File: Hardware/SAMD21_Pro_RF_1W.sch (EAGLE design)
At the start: 77 parts, among them J10 AVR_SPI_PROG_3X2TESTPOINTS, J12 JST, J13 U.FL, J14 RFM_DIO, J7 PTH, J9 External On/Off, U1 MCP73831, U2 ADJ3.3, U4 ATSAMD21G, U5 4MB Flash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

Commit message: Updates from board review
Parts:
- removed F2: 6V/0.75A, SparkFun-Fuses:PPTC_THREE-QUARTER-AMP
- removed J14: RFM_DIO, SparkFun-Connectors:CONN_06X2NO_SILK
- removed JP1, JP2: JUMPER-SMT_2_NO_SILK, SparkFun-Jumpers:JUMPER-SMT_2_NO_SILK
- removed JP3: JUMPER-SMT_3_1-NC_PASTE_SILK, SparkFun-Jumpers:JUMPER-SMT_3_1-NC_PASTE_SILK
- removed JP6: JUMPER-SMT_2_NC_PASTE_SILK, SparkFun-Jumpers:JUMPER-SMT_2_NC_PASTE_SILK
- removed LED2: RED, SparkFun-LED:LED-RED0603
- removed R12: 1k, SparkFun-Resistors:1KOHM-0603-1/10W-1%
- D4: value Yellow -> BLUE; device SparkFun-LED:LED-YELLOW0603 -> SparkFun-LED:LED-BLUE0603
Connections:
- removed net ANT_HEADER: J4.1, JP3.1
- removed net DIO0: J14.11, JP6.1, U8.A7
- removed net DIO1: J14.9, JP1.1, U8.A8
- removed net DIO2: J14.7, JP2.1, U9.A4
- removed net DIO3: J14.5, U9.A3
- removed net DIO35V: U6.DIO3, U9.B3
- removed net DIO4: J14.3, U9.A2
- removed net DIO45V: U6.DIO4, U9.B2
- removed net DIO5: J14.1, U9.A1
- removed net DIO55V: U6.DIO5, U9.B1
- removed net N$10: LED2.A, R12.1
- removed net N$3: J13.SIGNAL, JP3.3
- removed net N$4: F2.2, U2.IN
- net 5V: no longer R12.2
- net ANT: now also J13.SIGNAL, J4.1; no longer JP3.2
- net D10: now also U8.A8; no longer JP1.2
- net D11: now also U9.A4; no longer JP2.2
- net GND: no longer J14.10, J14.12, J14.2, J14.4, J14.6, J14.8, LED2.C
- net N$12: now also F1.1, SJ2.2; no longer F1.2, U7.IN
- net RAW: now also U2.IN, U7.IN; no longer F1.1, F2.1
- net RFM_INT: now also U8.A7; no longer JP6.2
- net USB_VCC: now also F1.2; no longer SJ2.2
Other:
- note added: "Elias Santistevan, Owen Lyke"
- note removed: "Close jumpers for LoRa WAN compatibility"
- note removed: "Elias Santistevan"
- note removed: "Pretty confident the E19 module uses the same base chip as the RFM (hope RF version) meaning that the DIO functions are the same"
- note removed: "Why were PB22 and PB23 left unconnected in other versions?"
- moved on the sheet: F1

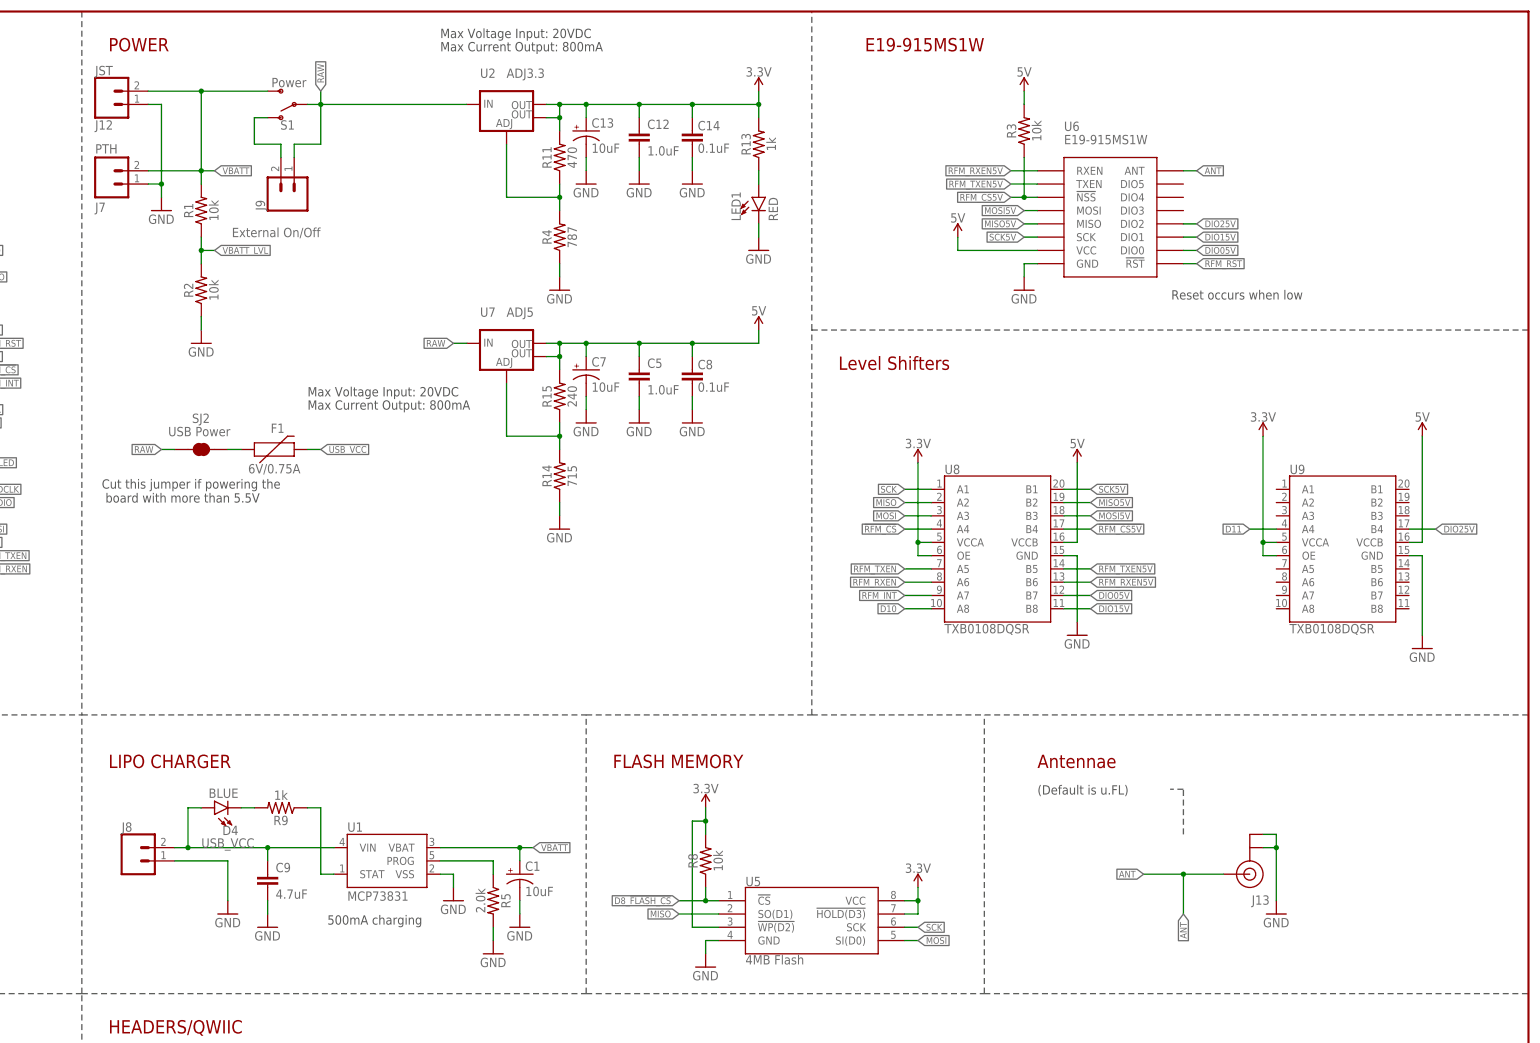
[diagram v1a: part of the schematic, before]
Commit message: Updated power supply in schematic
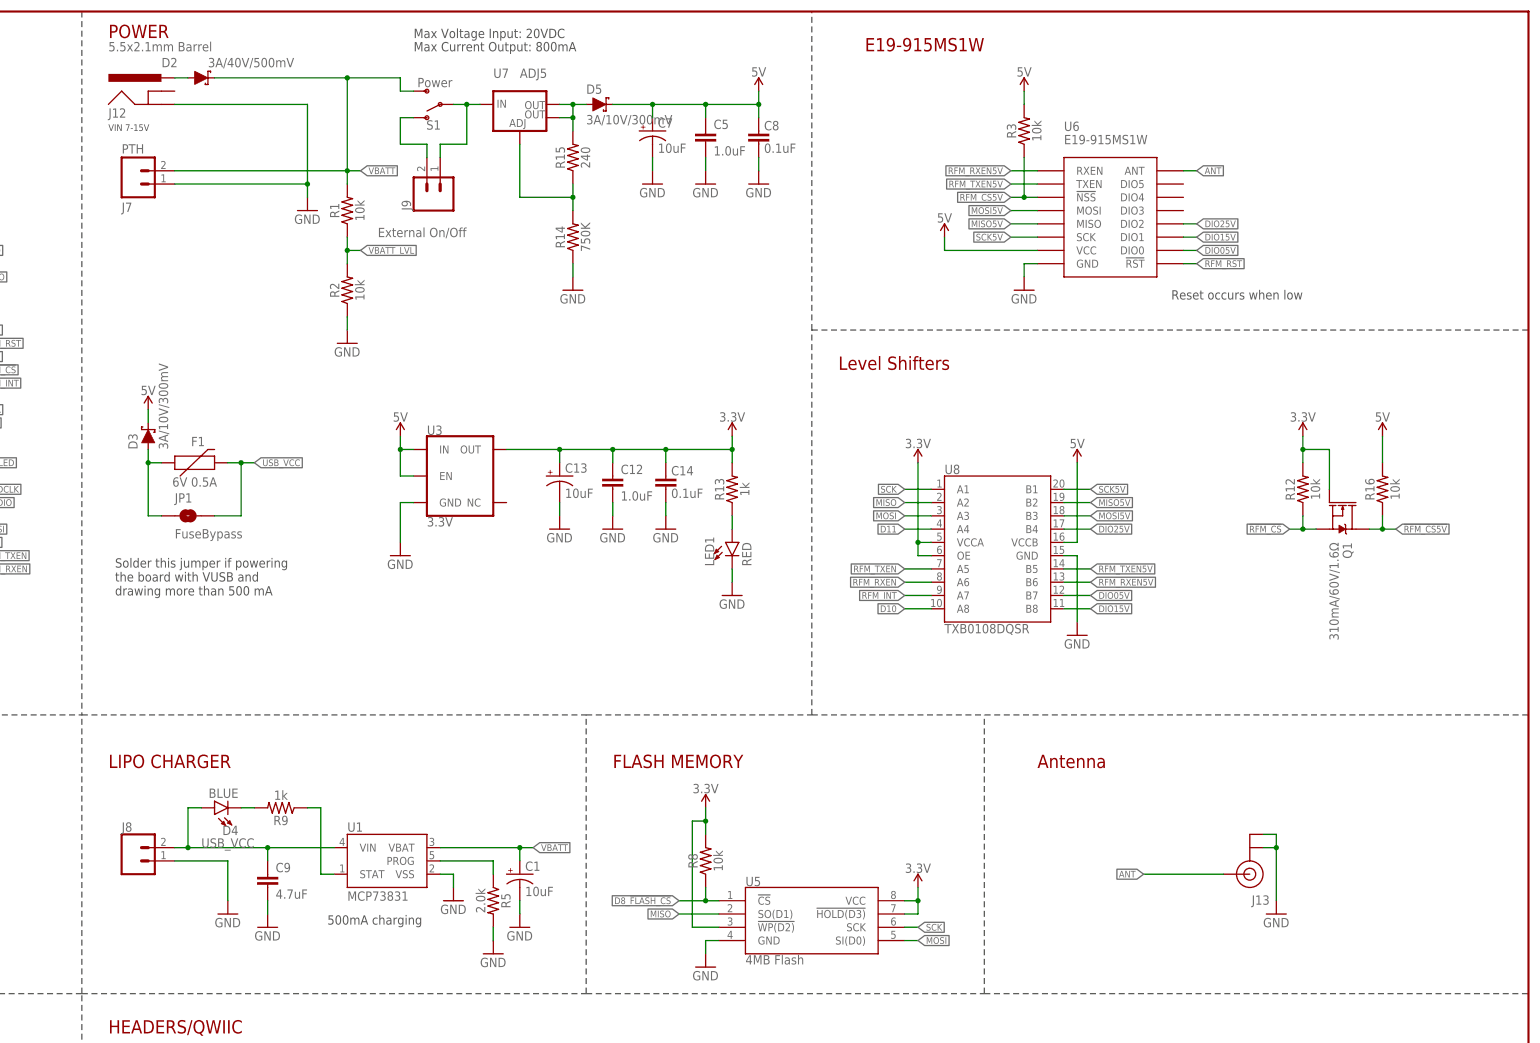
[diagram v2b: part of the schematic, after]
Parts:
- removed R11: 470, SparkFun-Resistors:470OHM-0603-1/10W-1%
- removed R4: 787, SparkFun-Resistors:787OHM-0603-1/10W-1%
- removed SJ2: USB Power, SparkFun-Jumpers:JUMPER-SMT_2_NC_TRACE_SILK
- removed U2: ADJ3.3, SparkFun-IC-Power:V_REG_LM1117SOT223
- removed U9: TXB0108DQSR, SparkFun-IC-Comms:TXB0108
- added D2: 3A/40V/500mV, SparkFun-DiscreteSemi:DIODE-SCHOTTKY-B340A
- added D3, D5: 3A/10V/300mV, SAMD21_ProRF_1W:DIODE-SCHOTTKY-BAT60A
- added JP1: FuseBypass, SparkFun-Jumpers:JUMPER-SMT_2_NO_SILK
- added Q1: 310mA/60V/1.6Ω, SparkFun-DiscreteSemi:MOSFET-NCH-2N7002PW
- added R12, R16: 10k, SparkFun-Resistors:10KOHM-0603-1/10W-1%
- added U3: 3.3V, SparkFun-IC-Power:V_REG_AP2112K-3.3V
- F1: value 6V/0.75A -> 6V 0.5A; device SparkFun-Fuses:PPTC_THREE-QUARTER-AMP -> SparkFun-Fuses:PPTC_6V500MA
- J12: value JST -> 5.5x2.1mm Barrel; device SparkFun-Connectors:CONN_02-JST-2MM-SMT -> SparkFun-Connectors:POWER_JACKSMD
- R14: value 715 -> 750K; device SparkFun-Resistors:715OHM-0603-1/10W-1% -> SparkFun-Resistors:750KOHM-0603-1/10W-1%
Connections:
- removed net N$5: R11.1, R4.2, U2.ADJ
- new net N$14: D5.A, R15.2, U7.OUT, U7.OUT@1
- new net N$4: D2.A, J12.PWR
- net !RFM_CS: now also Q1.S, R12.1; no longer U8.A4
- net !RFM_CS5V: now also Q1.D, R16.1; no longer U8.B4
- net 3.3V: now also Q1.G, R12.2, U3.OUT; no longer R11.2, U2.OUT, U2.OUT@1, U9.OE, U9.VCCA
- net 5V: now also D3.C, D5.C, R16.2, U3.EN, U3.IN; no longer R15.2, U7.OUT, U7.OUT@1, U9.VCCB
- net D11: now also U8.A4; no longer U9.A4
- net DIO25V: now also U8.B4; no longer U9.B4
- net GND: now also J12.GND, U3.GND; no longer J12.2, R4.1, U9.GND
- net N$12: now also D3.A, JP1.1; no longer SJ2.2
- net RAW: no longer SJ2.1, U2.IN
- net USB_VCC: now also JP1.2
- net VBATT: now also D2.C; no longer J12.1
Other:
- note added: "Antenna"
- note added: "Solder this jumper if powering the board with VUSB and drawing more than 500 mA"
- note added: "VIN 7-15V"
- note removed: "(Default is u.FL)"
- note removed: "Antennae"
- note removed: "Cut this jumper if powering the board with more than 5.5V"
- moved on the sheet: C12, C13, C14, C5, C7, C8, F1, J12, J7, J9, LED1, R1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

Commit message: Started a re-route
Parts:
- removed D2: 3A/40V/500mV, SparkFun-DiscreteSemi:DIODE-SCHOTTKY-B340A
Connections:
- removed net N$4: D2.A, J12.PWR
- net GND: now also J12.GNDBREAK
- net VBATT: now also J12.PWR; no longer D2.C
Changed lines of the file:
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@@
 <part name="GND21" library="SparkFun" deviceset="GND" device=""/>
 <part name="J12" library="SparkFun-Connectors" deviceset="POWER_JACK" device="SMD" value="5.5x2.1mm Barrel"/>
-<part name="D2" library="SparkFun-DiscreteSemi" deviceset="DIODE-SCHOTTKY" device="-B340A" value="3A/40V/500mV"/>
 <part name="Q1" library="SparkFun-DiscreteSemi" deviceset="MOSFET-NCH" device="-2N7002PW" value="310mA/60V/1.6Ω"/>
 <part name="R12" library="SparkFun-Resistors" deviceset="10KOHM" device="-0603-1/10W-1%" value="10k"/>
@@
 <attribute name="NAME" x="160.02" y="259.08" size="1.778" layer="95" font="vector"/>
 </instance>
-<instance part="D2" gate="G$1" x="177.8" y="266.7" smashed="yes">
-<attribute name="NAME" x="170.18" y="268.732" size="1.778" layer="95" font="vector"/>
-<attribute name="VALUE" x="195.58" y="268.732" size="1.778" layer="96" font="vector" rot="R180" align="top-left"/>
-</instance>
 <instance part="Q1" gate="NMOS" x="396.24" y="182.88" rot="R270"/>
 <instance part="R12" gate="G$1" x="388.62" y="187.96" rot="R90"/>
@@
 <junction x="198.12" y="246.38"/>
 <pinref part="J12" gate="G$1" pin="GND"/>
-<wire x1="172.72" y1="261.62" x2="198.12" y2="261.62" width="0.1524" layer="91"/>
+<wire x1="172.72" y1="261.62" x2="175.26" y2="261.62" width="0.1524" layer="91"/>
+<pinref part="J12" gate="G$1" pin="GNDBREAK"/>
+<wire x1="175.26" y1="261.62" x2="198.12" y2="261.62" width="0.1524" layer="91"/>
+<wire x1="172.72" y1="264.16" x2="175.26" y2="264.16" width="0.1524" layer="91"/>
+<wire x1="175.26" y1="264.16" x2="175.26" y2="261.62" width="0.1524" layer="91"/>
+<junction x="175.26" y="261.62"/>
 </segment>
 <segment>
@@
 <pinref part="S1" gate="1" pin="S"/>
 <wire x1="218.44" y1="264.16" x2="215.9" y2="264.16" width="0.1524" layer="91"/>
-<pinref part="D2" gate="G$1" pin="C"/>
-<wire x1="180.34" y1="266.7" x2="205.74" y2="266.7" width="0.1524" layer="91"/>
+<wire x1="172.72" y1="266.7" x2="205.74" y2="266.7" width="0.1524" layer="91"/>
 <wire x1="205.74" y1="266.7" x2="215.9" y2="266.7" width="0.1524" layer="91"/>
 <wire x1="215.9" y1="266.7" x2="215.9" y2="264.16" width="0.1524" layer="91"/>
 <junction x="205.74" y="266.7"/>
+<pinref part="J12" gate="G$1" pin="PWR"/>
 </segment>
 </net>
@@
 </segment>
 </net>
-<net name="N$4" class="0">
-<segment>
-<pinref part="J12" gate="G$1" pin="PWR"/>
-<wire x1="172.72" y1="266.7" x2="175.26" y2="266.7" width="0.1524" layer="91"/>
-<pinref part="D2" gate="G$1" pin="A"/>
-</segment>
-</net>
